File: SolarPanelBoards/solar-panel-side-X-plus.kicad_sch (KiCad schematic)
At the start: 56 parts, among them J1 Conn_01x06, U1 OPT3001DNPT

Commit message: updated sch
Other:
- note added: "I2C Protection"
- note removed: "IMU I2C Protection"
- moved on the sheet: C1, C?, H1, H2, H3, H4, H5, H6, H7, H8, J1, L?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

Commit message: Updated X-plus schematic and net
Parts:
- J1: value Conn_01x06 -> (none); footprint sapling:MOLEX_2053380006 -> (none)
- Q3, Q4: renamed from Q?; value BSS138DWQ-7 -> (none); footprint custom-footprints:BSS138DWQ-7 -> (none); symbol symbols:BSS138DWQ-7 -> sapling:BSS138DWQ-7
- SC6: value SM101K07TF -> (none); footprint sapling:SM101K07TF -> (none)
- U1: value OPT3001DNPT -> (none); footprint sapling:OPT3001 -> (none)
- U2: renamed from U?; value DRV8830DGQR -> (none); symbol xpanel-rescue:DRV8830DGQR-symbols -> sapling:symbols_DRV8830DGQR
- gave numbers to parts that had none: 25
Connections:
- net GND: now also Q4.1 (S2), Q4.4 (S1); no longer Q4.1 (S2), Q4.4 (S1), U2.11 (EP)
- net SCL: now also Q1.4 (E2), Q1.6 (C1)
- net SCL1_b4iso: now also Q1.1 (E1), Q1.3 (C2)
- net SDA: now also Q2.4 (E2), Q2.6 (C1)
- net SDA1_b4iso: now also Q2.1 (E1), Q2.3 (C2)
- net at Q3.6 (D1), R1.2, R5.1: now also Q1.5 (B2)
- net at R2.2, R6.2: now also Q2.5 (B2), Q4.6 (D1); no longer Q4.3 (D2)
- net at R6.1: now also Q2.2 (B1)
- net at C3.1, R10.1: now also Q4.5 (G1); no longer Q4.2 (G2)
- net at R5.2: now also Q1.2 (B1)
- new net: Q4.2 (G2), Q4.3 (D2), R8.1

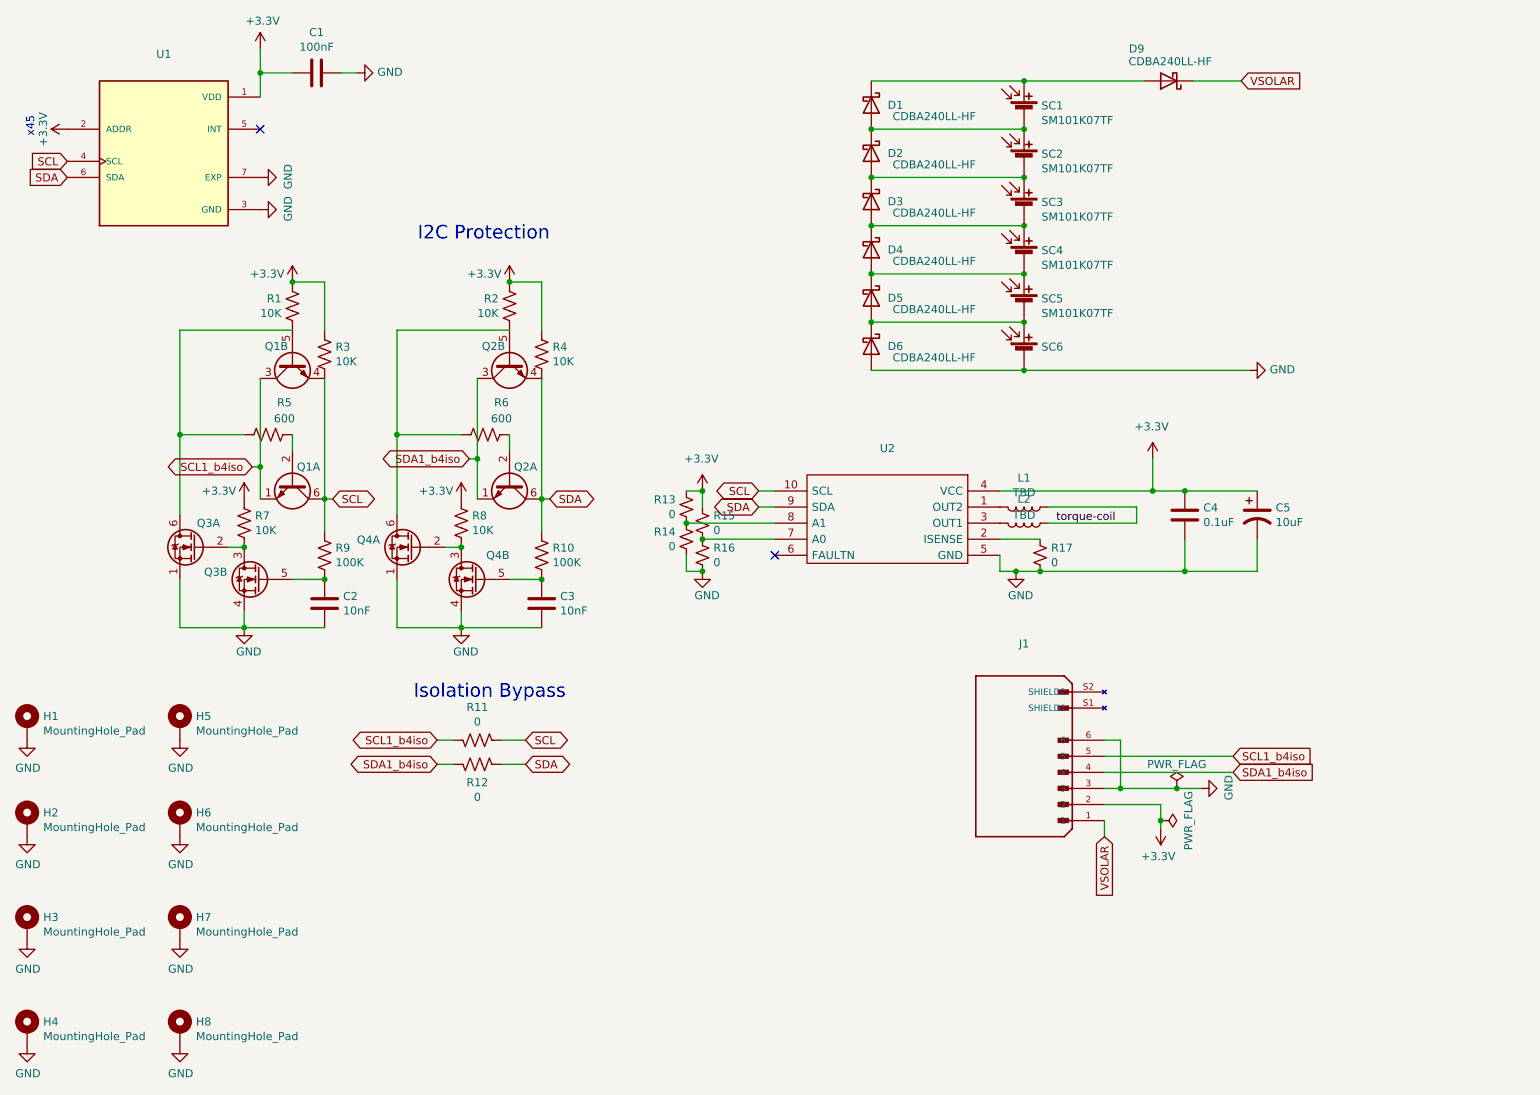
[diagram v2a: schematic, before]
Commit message: Updated X-plus schematic, netlist, PCB, and gerbers
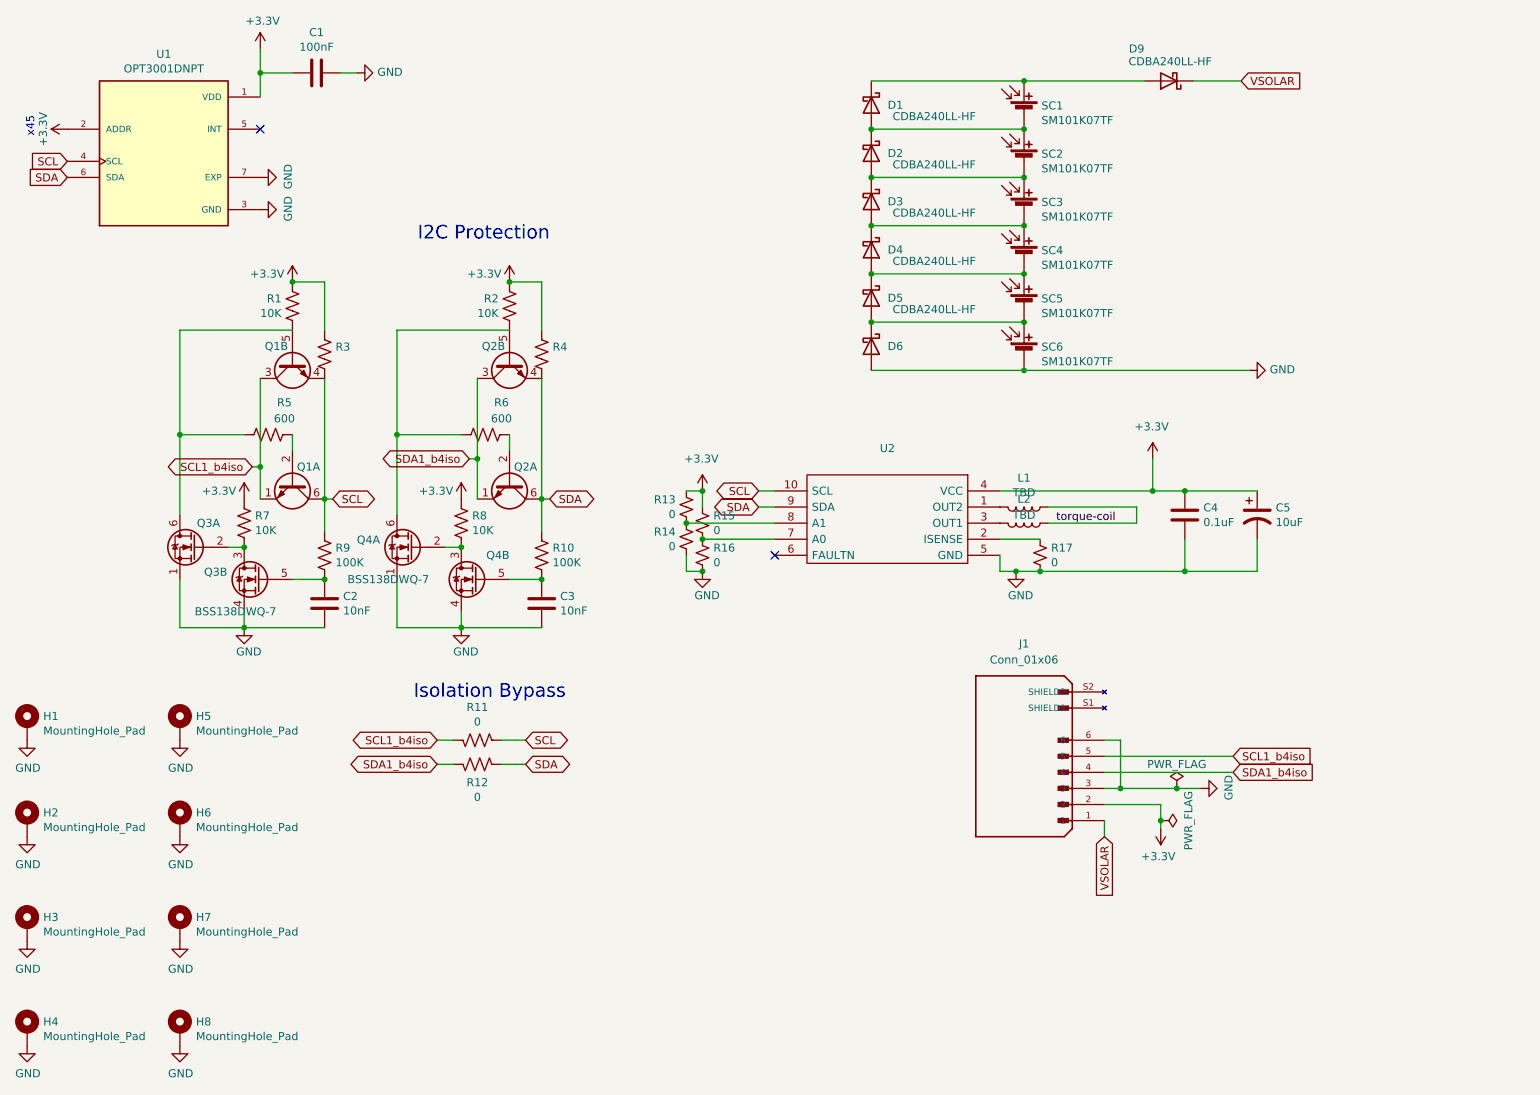
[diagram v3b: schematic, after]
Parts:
- D6: value CDBA240LL-HF -> (none); footprint sapling:DO-214AC -> (none)
- J1: value (none) -> Conn_01x06; footprint (none) -> sapling:MOLEX_2053380006
- Q3, Q4: value (none) -> BSS138DWQ-7; footprint (none) -> sapling:BSS138DWQ-7
- R3, R4: value 10K -> (none); footprint Resistor_SMD:R_0402_1005Metric -> (none)
- SC6: value (none) -> SM101K07TF; footprint (none) -> sapling:SM101K07TF
- U1: value (none) -> OPT3001DNPT; footprint (none) -> sapling:OPT3001
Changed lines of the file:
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@@
     (in_bom yes) (on_board yes)
     (property "Reference" "D6" (id 0) (at 167.64 72.39 90))
-    (property "Value" "CDBA240LL-HF" (id 1) (at 180.34 74.93 90)
+    (property "Value" "" (id 1) (at 180.34 74.93 90)
       (effects (font (size 1.27 1.27)) (justify right bottom))
     )
-    (property "Footprint" "sapling:DO-214AC" (id 2) (at 163.83 72.39 0)
+    (property "Footprint" "" (id 2) (at 163.83 72.39 0)
       (effects (font (size 1.27 1.27)) hide)
     )
@@
       (effects (font (size 1.27 1.27)) (justify left))
     )
-    (property "Value" "" (id 1) (at 190.7032 74.803 0)
-      (effects (font (size 1.27 1.27)) (justify left))
-    )
-    (property "Footprint" "" (id 2) (at 187.96 72.136 90)
+    (property "Value" "SM101K07TF" (id 1) (at 190.7032 74.803 0)
+      (effects (font (size 1.27 1.27)) (justify left))
+    )
+    (property "Footprint" "sapling:SM101K07TF" (id 2) (at 187.96 72.136 90)
       (effects (font (size 1.27 1.27)) hide)
     )
@@
     (in_bom yes) (on_board yes)
     (property "Reference" "J1" (id 0) (at 187.96 119.38 0))
-    (property "Value" "" (id 1) (at 187.96 121.92 0))
-    (property "Footprint" "" (id 2) (at 187.96 137.16 0)
+    (property "Value" "Conn_01x06" (id 1) (at 187.96 121.92 0))
+    (property "Footprint" "sapling:MOLEX_2053380006" (id 2) (at 187.96 137.16 0)
       (effects (font (size 1.27 1.27)) hide)
     )
@@
     (in_bom yes) (on_board yes)
     (property "Reference" "U1" (id 0) (at 52.07 26.2382 0))
-    (property "Value" "" (id 1) (at 52.07 28.5496 0))
-    (property "Footprint" "" (id 2) (at 46.99 27.94 0)
+    (property "Value" "OPT3001DNPT" (id 1) (at 52.07 28.5496 0))
+    (property "Footprint" "sapling:OPT3001" (id 2) (at 46.99 27.94 0)
       (effects (font (size 1.27 1.27)) (justify left bottom) hide)
     )
@@
       (effects (font (size 1.27 1.27)) (justify right))
     )
-    (property "Value" "10K" (id 1) (at 113.4872 74.803 0)
-      (effects (font (size 1.27 1.27)) (justify right))
-    )
-    (property "Footprint" "Resistor_SMD:R_0402_1005Metric" (id 2) (at 110.744 73.406 90)
+    (property "Value" "" (id 1) (at 113.4872 74.803 0)
+      (effects (font (size 1.27 1.27)) (justify right))
+    )
+    (property "Footprint" "" (id 2) (at 110.744 73.406 90)
       (effects (font (size 1.27 1.27)) hide)
     )
@@
       (effects (font (size 1.27 1.27)) (justify left))
     )
-    (property "Value" "" (id 1) (at 69.85 114.3 0)
-      (effects (font (size 1.27 1.27)) (justify left))
-    )
-    (property "Footprint" "" (id 2) (at 62.23 105.41 0)
+    (property "Value" "BSS138DWQ-7" (id 1) (at 69.85 114.3 0)
+      (effects (font (size 1.27 1.27)) (justify left))
+    )
+    (property "Footprint" "sapling:BSS138DWQ-7" (id 2) (at 62.23 105.41 0)
       (effects (font (size 1.27 1.27)) (justify left) hide)
     )
@@
       (effects (font (size 1.27 1.27)) (justify left))
     )
-    (property "Value" "" (id 1) (at 96.393 110.363 0)
-      (effects (font (size 1.27 1.27)) (justify left) hide)
-    )
-    (property "Footprint" "" (id 2) (at 96.52 105.41 0)
+    (property "Value" "BSS138DWQ-7" (id 1) (at 96.393 110.363 0)
+      (effects (font (size 1.27 1.27)) (justify left) hide)
+    )
+    (property "Footprint" "sapling:BSS138DWQ-7" (id 2) (at 96.52 105.41 0)
       (effects (font (size 1.27 1.27)) (justify left) hide)
     )
@@
       (effects (font (size 1.27 1.27)) (justify left))
     )
-    (property "Value" "" (id 1) (at 51.943 105.283 0)
-      (effects (font (size 1.27 1.27)) (justify left) hide)
-    )
-    (property "Footprint" "" (id 2) (at 52.07 100.33 0)
+    (property "Value" "BSS138DWQ-7" (id 1) (at 51.943 105.283 0)
+      (effects (font (size 1.27 1.27)) (justify left) hide)
+    )
+    (property "Footprint" "sapling:BSS138DWQ-7" (id 2) (at 52.07 100.33 0)
       (effects (font (size 1.27 1.27)) (justify left) hide)
     )
@@
       (effects (font (size 1.27 1.27)) (justify left))
     )
-    (property "Value" "" (id 1) (at 93.98 109.22 0)
-      (effects (font (size 1.27 1.27)) (justify left))
-    )
-    (property "Footprint" "" (id 2) (at 86.36 100.33 0)
+    (property "Value" "BSS138DWQ-7" (id 1) (at 93.98 109.22 0)
+      (effects (font (size 1.27 1.27)) (justify left))
+    )
+    (property "Footprint" "sapling:BSS138DWQ-7" (id 2) (at 86.36 100.33 0)
       (effects (font (size 1.27 1.27)) (justify left) hide)
     )
@@
       (effects (font (size 1.27 1.27)) (justify right))
     )
-    (property "Value" "10K" (id 1) (at 79.1972 74.803 0)
-      (effects (font (size 1.27 1.27)) (justify right))
-    )
-    (property "Footprint" "Resistor_SMD:R_0402_1005Metric" (id 2) (at 76.454 73.406 90)
+    (property "Value" "" (id 1) (at 79.1972 74.803 0)
+      (effects (font (size 1.27 1.27)) (justify right))
+    )
+    (property "Footprint" "" (id 2) (at 76.454 73.406 90)
       (effects (font (size 1.27 1.27)) hide)
     )
@@
     )
     (path "/ec53b93c-c93c-4a00-b315-00a9db4c857c"
-      (reference "R3") (unit 1) (value "10K") (footprint "Resistor_SMD:R_0402_1005Metric")
+      (reference "R3") (unit 1) (value "10K") (footprint "Resistor_SMD:R_0603_1608Metric")
     )
     (path "/0f122926-6ab0-4321-bb42-3042bba502d6"
-      (reference "R4") (unit 1) (value "10K") (footprint "Resistor_SMD:R_0402_1005Metric")
+      (reference "R4") (unit 1) (value "10K") (footprint "Resistor_SMD:R_0603_1608Metric")
     )
     (path "/8b7bd606-8d7f-4fbd-a2d5-a4d4e067ee34"
@@
     )
     (path "/b85d2401-b9b9-4c27-b2e2-c9d9ab116d00"
-      (reference "U2") (unit 1) (value "DRV8830DGQR") (footprint "custom-footprints:DRV8830DGQR")
-    )
-  )
+      (reference "U2") (unit 1) (value "DRV8830DGQR") (footprint "sapling:DRV8830DGQ")
+    )
+  )
